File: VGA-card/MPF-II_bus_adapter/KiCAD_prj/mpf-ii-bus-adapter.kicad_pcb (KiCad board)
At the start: 2 copper layers, 98.5 x 35.6 mm, 35 parts, among them J1 Bus_Apple_II_Card_Side, J10 USER1_Sel, J11 INH_Sel, J12 RDY_Sel, J13 COLREF_Sel, J14 IOSTRB_Sel, J15 Q3_Sel, J16 Pin, J17 Pin, J18 Pin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

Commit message: New PCB started
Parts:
- removed C4: 0.1u, Capacitor_THT:C_Disc_D4.3mm_W1.9mm_P5.00mm
- added C5: 0.1u, Capacitor_THT:C_Disc_D4.3mm_W1.9mm_P5.00mm, F.Cu at (191.2, 63.0)
- moved J10 70.9 mm to (197.7, 82.2)
- moved J12 70.9 mm to (249.1, 82.3)
- moved J13 70.9 mm to (208.2, 84.7)
- moved J14 70.9 mm to (228.0, 84.8)
- moved J15 70.9 mm to (203.0, 82.2)
- moved J26 70.9 mm to (218.5, 84.7)
- moved J5 70.9 mm to (213.5, 84.7)
- moved J6 70.9 mm to (223.0, 82.3)
- moved J7 70.9 mm to (243.6, 82.3)
- moved J8 70.9 mm to (254.0, 82.3)
- moved J9 70.9 mm to (233.1, 82.3)
- moved J11 70.9 mm to (238.3, 82.3)
- moved J2 69.2 mm to (136.8, 27.5)
- moved J3 53.0 mm to (117.1, 45.8)
- moved U1 47.3 mm to (54.5, 83.3)
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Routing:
- net GND: track 172.5 -> 0.23 mm
- net +5V: track 152.0 -> 0.00 mm
- net /PHI1: track 87.8 -> 0.00 mm, vias 1 -> 0
- net /M_DEVSEL: track 54.5 -> 0.00 mm, vias 2 -> 0
- net /PHI2: track 43.6 -> 0.00 mm
- net Net-(J4-Pin_1): track 35.2 -> 0.00 mm
- net /RESET: track 32.5 -> 0.00 mm
- net /D3: track 31.2 -> 0.00 mm
- net /D2: track 30.1 -> 0.00 mm
- net -5V: track 29.8 -> 0.00 mm
- net /2M: track 29.1 -> 0.00 mm, vias 2 -> 0
- net /D5: track 28.9 -> 0.00 mm
- net +12V: track 28.9 -> 0.00 mm
- net /D7: track 28.7 -> 0.00 mm
- net /INTIN: track 28.5 -> 0.00 mm
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- removed copper zone on B.Cu, net GND
- removed copper zone on F.Cu, net GND

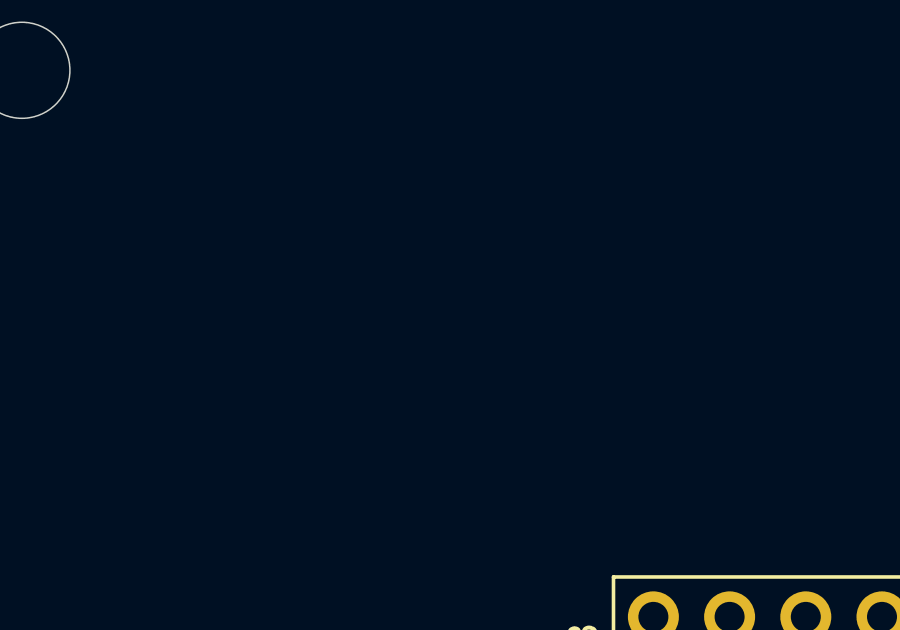
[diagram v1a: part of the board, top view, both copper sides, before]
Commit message: Schematics connections list updated
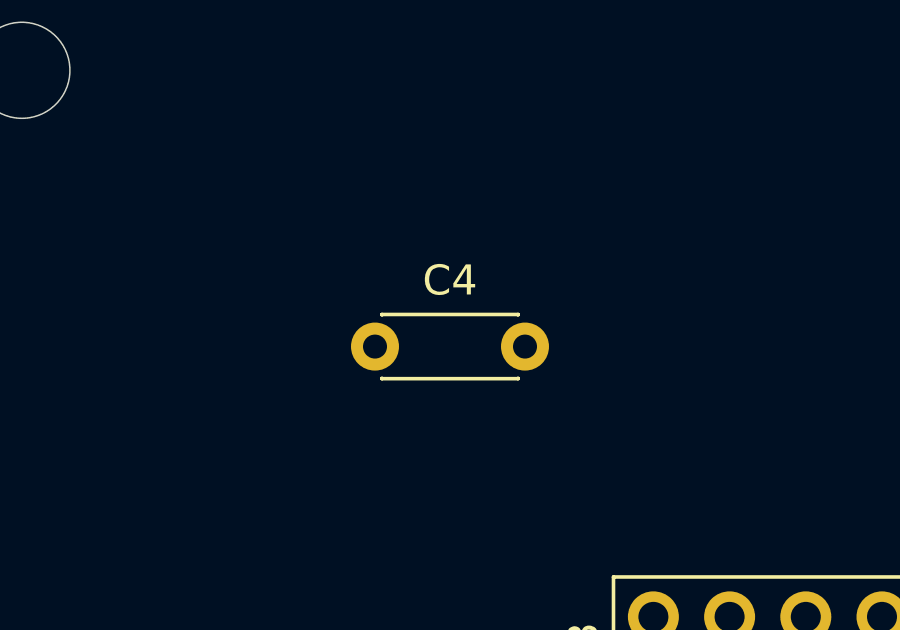
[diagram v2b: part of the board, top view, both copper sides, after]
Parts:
- added C4: 0.1u, Capacitor_THT:C_Disc_D4.3mm_W1.9mm_P5.00mm, F.Cu at (109.9, 89.5)
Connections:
- net /A_DEVSEL renamed /DEVSEL
- net /A_USER1 renamed /USER1
- net /M_DEVSEL renamed /EXTC

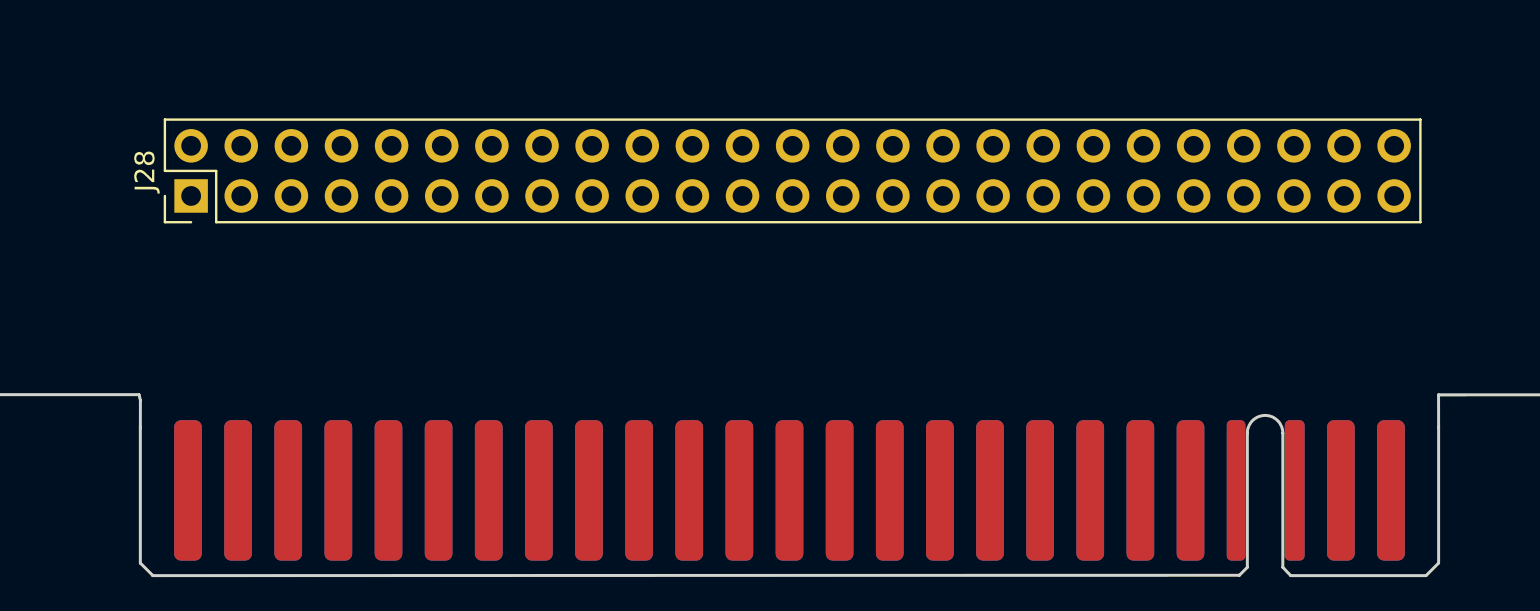
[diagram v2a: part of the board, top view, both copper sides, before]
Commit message: PCB connector updated
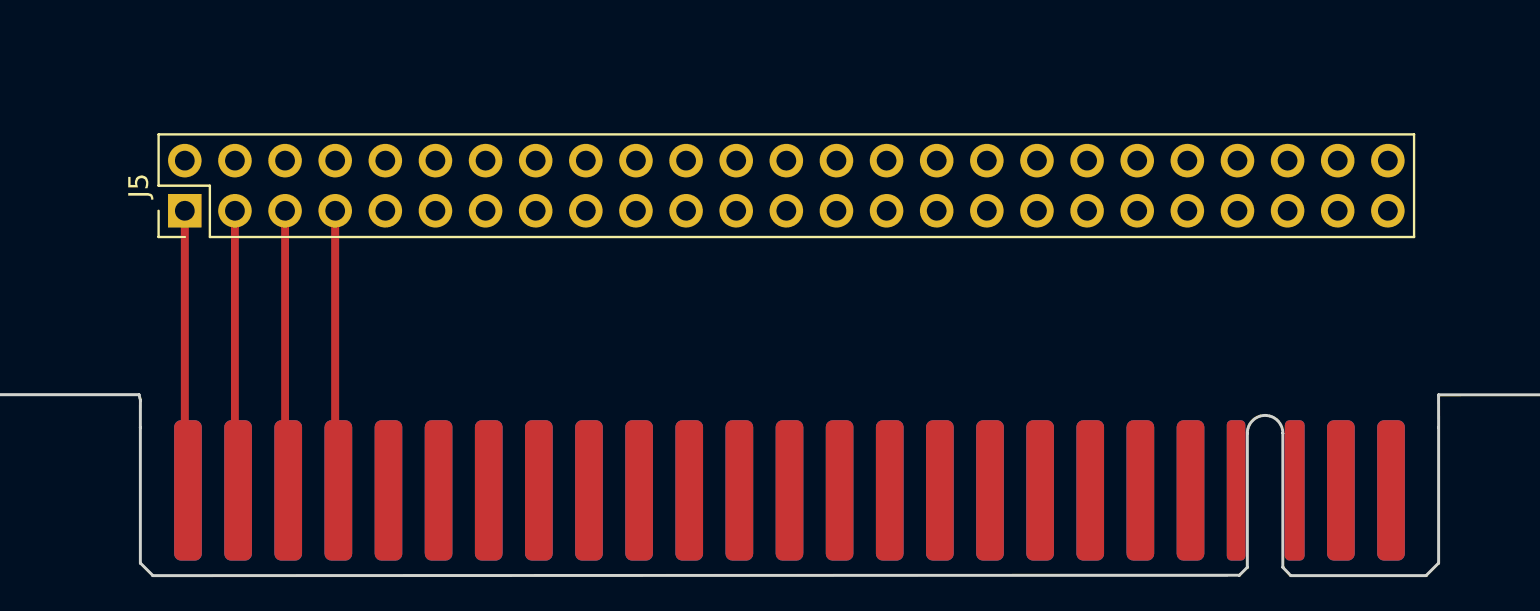
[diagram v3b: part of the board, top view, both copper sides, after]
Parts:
- removed J28: MPF-Bus, Connector_PinHeader_2.54mm:PinHeader_2x25_P2.54mm_Vertical
- added J5: Conn_02x25_Odd_Even, Connector_PinHeader_2.54mm:PinHeader_2x25_P2.54mm_Vertical, F.Cu at (118.8, 101.8)
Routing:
- net /IOSEL: track 0.74 -> 15.0 mm
- net /A2: track 0.00 -> 14.2 mm
- net /A1: track 0.00 -> 14.2 mm
- net /A0: track 3.36 -> 17.6 mm

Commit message: PCB updated
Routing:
- net +12V: track 0.00 -> 18.9 mm
- net /D4: track 0.00 -> 17.9 mm
- net /D2: track 0.00 -> 17.9 mm
- net /SOUND_IN: track 0.00 -> 17.9 mm
- net /2M: track 0.00 -> 17.9 mm
- net /PHI1: track 0.00 -> 17.9 mm
- net /INTIN: track 0.00 -> 17.9 mm
- net GND: track 0.23 -> 18.1 mm
- net /DMAIN: track 0.00 -> 17.8 mm
- net /IODIS: track 0.00 -> 17.8 mm
- net /PHI2: track 0.00 -> 17.8 mm
- net -5V: track 0.00 -> 17.8 mm
- net /EXTC: track 0.00 -> 17.8 mm
- net /EXT6: track 0.00 -> 17.7 mm
- net /RESET: track 0.00 -> 17.7 mm
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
